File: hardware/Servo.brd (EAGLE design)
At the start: 45.7 x 58.2 mm, 13 parts, among them Q1 AOD417, U1 PCA9685

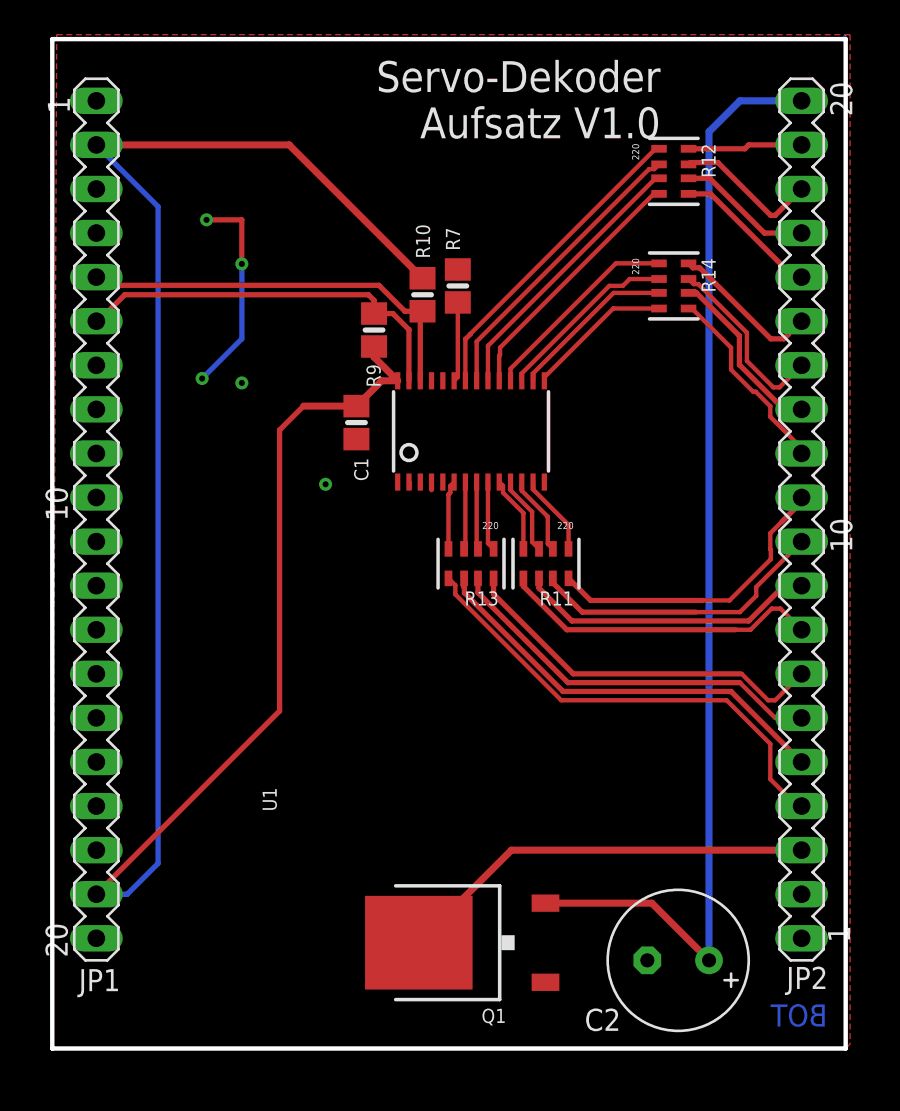
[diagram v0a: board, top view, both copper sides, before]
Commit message: Wiederstände als 0803
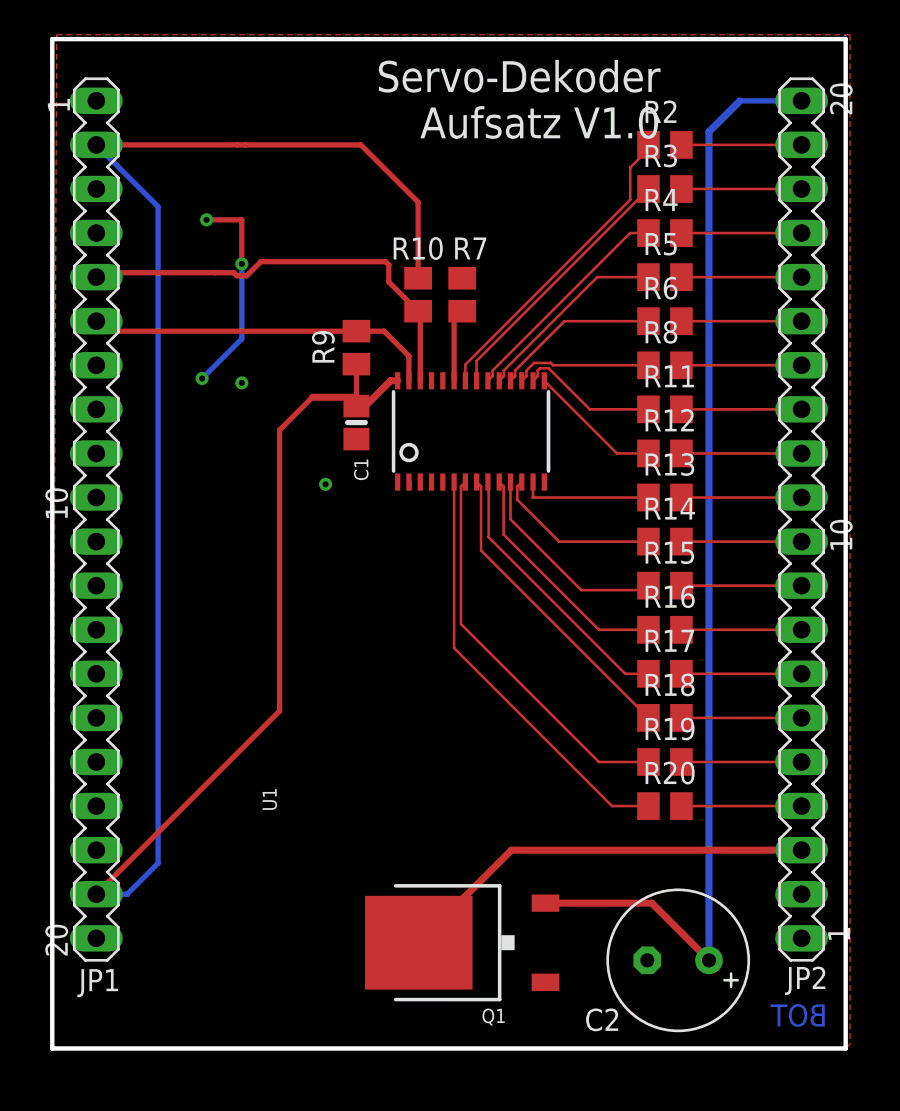
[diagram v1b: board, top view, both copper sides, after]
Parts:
- added R15, R16, R17, R18, R19, R2, R20, R3, R4, R5, R6, R8: 220, rcl:M0805
- C2: value 470µF -> 1000µF
- R10, R7, R9: device microbuilder:0805-NO -> rcl:M0805
- R11, R12, R13, R14: device microbuilder:RESPACK_4X0603 -> rcl:M0805
- moved R12 16.3 mm to (35.3, 34.5), turned to 0 degrees
- moved R14 14.7 mm to (35.3, 29.5), turned to 0 degrees
- moved R13 11.8 mm to (35.3, 32.0), turned to 0 degrees
- moved R11 11.2 mm to (35.3, 37.1), turned to 0 degrees
- moved R9 1.44 mm to (17.5, 40.6)
- moved R7 0.57 mm to (23.6, 43.7)
- moved R10 0.25 mm to (21.1, 43.7)
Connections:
- removed net 5.0V: C2.+, JP2.20, Q1.2
- new net +5VPIN3: JP2.3, Q1.3
- net +5V: now also C2.+, JP2.20, Q1.2; no longer JP2.3, Q1.3
- net N$10: now also R6.2; no longer R14.8
- net N$11: now also R8.2; no longer R14.7
- net N$12: now also R3.2; no longer R12.7
- net N$13: now also R11.2; no longer R14.6
- net N$14: now also R2.2; no longer R12.8
- net N$15: now also R16.2; no longer R11.5
- net N$17: now also R5.2; no longer R12.5
- net N$18: now also R12.2; no longer R14.5
- net N$2: now also R4.2; no longer R12.6
- net N$3: now also R13.2; no longer R11.8
- net N$4: now also R14.2; no longer R11.7
- net N$5: now also R15.2; no longer R11.6
- net N$6: now also R17.2; no longer R13.8
- net N$7: now also R18.2; no longer R13.7
- net N$8: now also R19.2; no longer R13.6
- net N$9: now also R20.2; no longer R13.5
- net PWM0: now also R20.1; no longer R13.4
- net PWM1: now also R19.1; no longer R13.3
- net PWM10: now also R8.1; no longer R14.2
- net PWM11: now also R6.1; no longer R14.1
- net PWM12: now also R5.1; no longer R12.4
- net PWM13: now also R4.1; no longer R12.3
- net PWM14: now also R3.1; no longer R12.2
- net PWM15: now also R2.1; no longer R12.1
- net PWM2: now also R18.1; no longer R13.2
- net PWM3: now also R17.1; no longer R13.1
- net PWM4: now also R16.1; no longer R11.4
- net PWM5: now also R15.1; no longer R11.3
- net PWM6: now also R14.1; no longer R11.2
- net PWM7: now also R13.1; no longer R11.1
- net PWM8: now also R12.1; no longer R14.4
- net PWM9: now also R11.1; no longer R14.3
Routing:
- net 5.0V: track 64.6 -> 0.00 mm
- net +5V: track 24.3 -> 64.6 mm
- net +5VPIN3: track 0.00 -> 24.3 mm
- net PWM0: track 3.99 -> 24.5 mm
- net N$9: track 27.3 -> 6.92 mm
- net PWM1: track 3.88 -> 22.4 mm
- net N$8: track 24.3 -> 6.92 mm
- net N$7: track 22.5 -> 6.92 mm
- net N$6: track 21.8 -> 6.92 mm
- net PWM2: track 3.88 -> 17.7 mm
- net PWM3: track 3.99 -> 15.7 mm
- net N$15: track 18.5 -> 6.92 mm
- net N$3: track 17.5 -> 6.92 mm
- net N$5: track 17.3 -> 6.92 mm
- net N$4: track 17.3 -> 6.92 mm
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
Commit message: Neue Version V2 des ServoAufsatzes
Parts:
- removed Q1: AOD417, microbuilder:TO252
- added Q2: IRLML6401, microbuilder:SOT23-WIDE
- moved C2 8.65 mm to (27.4, 4.83), turned to 270 degrees
- renumbered U1 to PCA9685
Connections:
- net +5V: now also Q2.2; no longer Q1.2
- net +5VPIN3: now also Q2.3; no longer Q1.3
- net GND: now also Q2.1; no longer Q1.1
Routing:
- net +5VPIN3: track 24.3 -> 8.41 mm
- net GND: track 12.5 -> 14.9 mm
- net SDA: track 20.3 -> 22.4 mm
- net +5V: track 64.6 -> 66.4 mm
- net SCL: track 24.9 -> 23.4 mm
